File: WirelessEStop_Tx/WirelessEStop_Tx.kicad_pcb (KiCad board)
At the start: 2 copper layers, 99.1 x 99.1 mm, 0 parts

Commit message: Worked on Board Layout
Pretty much finished the board. Need the BOM and stuff yet.
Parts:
- added C1: 10u, Capacitor_SMD:C_0603_1608Metric_Pad1.05x0.95mm_HandSolder, F.Cu at (127.5, 97.0)
- added C2: 10u, Capacitor_SMD:C_0603_1608Metric_Pad1.05x0.95mm_HandSolder, F.Cu at (113.3, 95.5)
- added Conn1: 9V Batt, MRDT_Connectors:MOLEX_SL_02_Horizontal, B.Cu at (139.2, 78.1)
- added D0: 3.3V_Schottky, Diode_SMD:D_0603_1608Metric_Pad1.05x0.95mm_HandSolder, F.Cu at (119.8, 101.6)
- added D1: LED, LED_SMD:LED_0603_1608Metric_Pad1.05x0.95mm_HandSolder, F.Cu at (135.3, 112.0)
- added D2: LED, LED_SMD:LED_0603_1608Metric_Pad1.05x0.95mm_HandSolder, F.Cu at (142.5, 112.0)
- added D3: LED, LED_SMD:LED_0603_1608Metric_Pad1.05x0.95mm_HandSolder, F.Cu at (149.5, 112.0)
- added D4: LED, LED_SMD:LED_0603_1608Metric_Pad1.05x0.95mm_HandSolder, F.Cu at (156.8, 112.0)
- added D5: LED, LED_SMD:LED_0603_1608Metric_Pad1.05x0.95mm_HandSolder, F.Cu at (152.0, 89.7)
- added G***: LOGO, MRDT_Silkscreens:MRDT_Logo_20mm, F.Cu at (177.3, 87.6)
- added L1: 47uH Inductor, WirelessEStop:ETQ-P4M470YFN_Inductor, F.Cu at (127.4, 101.6)
- added R1: 10K, Resistor_SMD:R_0603_1608Metric_Pad1.05x0.95mm_HandSolder, F.Cu at (121.9, 112.7)
- added R2: 10K, Resistor_SMD:R_0603_1608Metric_Pad1.05x0.95mm_HandSolder, F.Cu at (121.9, 116.3)
- added R3: 500, Resistor_SMD:R_0603_1608Metric_Pad1.05x0.95mm_HandSolder, F.Cu at (142.5, 116.3)
- added R4: 500, Resistor_SMD:R_0603_1608Metric_Pad1.05x0.95mm_HandSolder, F.Cu at (149.6, 116.3)
- added R5: 500, Resistor_SMD:R_0603_1608Metric_Pad1.05x0.95mm_HandSolder, F.Cu at (156.7, 116.3)
- added R6: 500, Resistor_SMD:R_0603_1608Metric_Pad1.05x0.95mm_HandSolder, F.Cu at (152.1, 92.7)
- added R7: 500, Resistor_SMD:R_0603_1608Metric_Pad1.05x0.95mm_HandSolder, F.Cu at (135.4, 115.7)
- added SW1: MOM Switch, WirelessEStop:D6_SPST, F.Cu at (154.7, 73.3)
- added SW2: Maintain Switch, WirelessEStop:ToggleSwitch_SPDT, F.Cu at (172.6, 105.7)
- added SW3: Master Power, WirelessEStop:SlideSwitch_SPST, F.Cu at (98.3, 97.8)
- added U1: ESP_8266_01, WirelessEStop:ESP8266-01, F.Cu at (96.3, 117.9)
- added U2: AP1059, Package_SO:SOIC-8_3.9x4.9mm_P1.27mm, F.Cu at (113.3, 99.6)
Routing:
- net +3V3: track 0.00 -> 186.5 mm, vias 0 -> 6
- net Maintain_IN: track 0.00 -> 118.0 mm, vias 0 -> 2
- net MOM_IN: track 0.00 -> 100.8 mm, vias 0 -> 2
- net SW_EStop: track 0.00 -> 74.6 mm, vias 0 -> 4
- net /Vin: track 0.00 -> 53.5 mm
- net SW_Link_EN: track 0.00 -> 43.8 mm
- net Net-(D0-Pad1): track 0.00 -> 20.1 mm
- net Net-(C2-Pad2): track 0.00 -> 16.2 mm
- net Net-(D5-Pad1): track 0.00 -> 3.09 mm
- net Net-(D4-Pad1): track 0.00 -> 2.61 mm
- net Net-(D3-Pad1): track 0.00 -> 2.61 mm
- net Net-(D2-Pad1): track 0.00 -> 2.57 mm
- net Net-(D1-Pad1): track 0.00 -> 1.97 mm
- net GND: track 0.00 -> 0.41 mm, vias 0 -> 19
- added copper zone on B.Cu, net GND
- added copper zone on F.Cu, net GND
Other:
- board text added: "Dead Man's SW"
- board text added: "EStop"
- board text added: "Enable Estop"
- board text added: "Enable Estop SW"
- board text added: "Main Power"
- board text added: "Power"
- board text added: "Wifi Connection"

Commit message: Fixed Board
Changed AP1509 and fixed the ESP8266-01
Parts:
- removed D0: 3.3V_Schottky, Diode_SMD:D_0603_1608Metric_Pad1.05x0.95mm_HandSolder
- removed G***: LOGO, MRDT_Silkscreens:MRDT_Logo_20mm
- removed L1: 47uH Inductor, WirelessEStop:ETQ-P4M470YFN_Inductor
- U2: value AP1059 -> OKI; footprint Package_SO:SOIC-8_3.9x4.9mm_P1.27mm -> MRDT_Devices:OKI_Horizontal
- moved C1 9.98 mm to (120.5, 104.1)
- moved U2 9.16 mm to (121.9, 102.6), turned to 180 degrees
- moved C2 8.64 mm to (113.4, 104.1)
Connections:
- C1 pad 1: +3V3 -> GND
- C1 pad 2: GND -> Net-(C1-Pad2)
- C2 pad 2: Net-(C2-Pad2) -> +3V3
- SW3 pad 1: Net-(C2-Pad2) -> Net-(C1-Pad2)
- U2 pad 1: Net-(C2-Pad2) -> Net-(C1-Pad2)
- U2 pad 2: Net-(D0-Pad1) -> GND
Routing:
- net Net-(C1-Pad2): track 0.00 -> 27.4 mm
- net Maintain_IN: track 118.0 -> 97.5 mm
- net SW_EStop: track 74.6 -> 95.0 mm
- net Net-(D0-Pad1): track 20.1 -> 0.00 mm
- net Net-(C2-Pad2): track 16.2 -> 0.00 mm
- net +3V3: track 186.5 -> 191.1 mm, vias 6 -> 2
- net SW_Link_EN: track 43.8 -> 46.5 mm
- net MOM_IN: track 100.8 -> 99.5 mm
- net GND: track 0.41 -> 0.00 mm, vias 19 -> 14

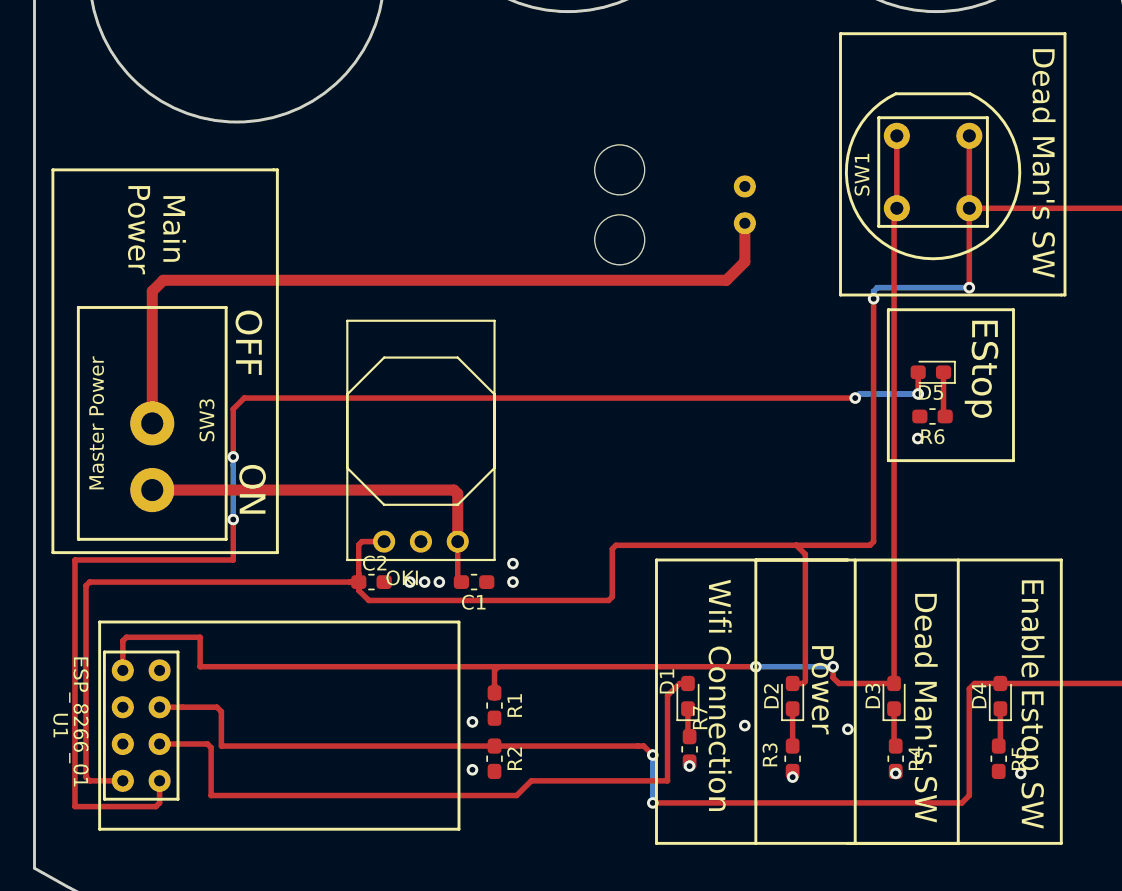
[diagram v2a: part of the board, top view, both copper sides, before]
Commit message: Updated BOM
Fixed the items on the BOM
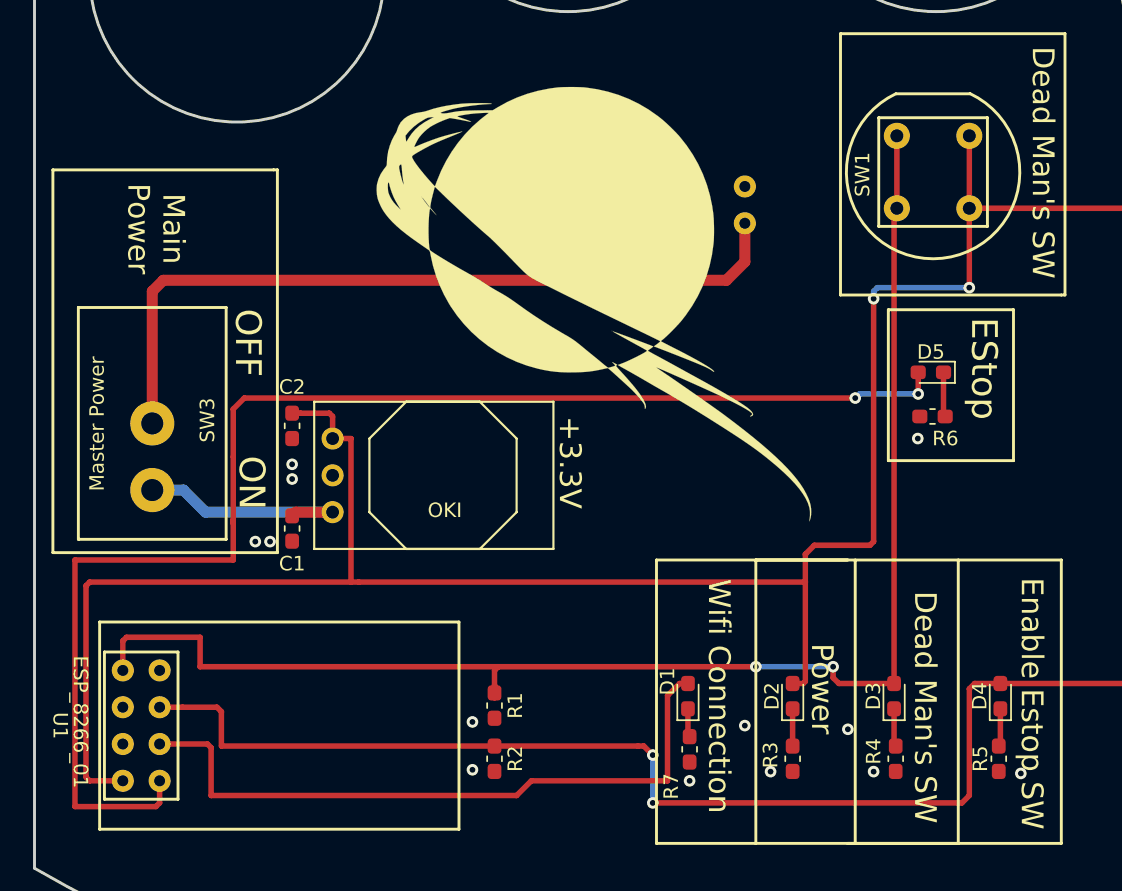
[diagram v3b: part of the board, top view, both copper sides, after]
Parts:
- added G***: LOGO, MRDT_Silkscreens:MRDT_Logo_30mm, F.Cu at (128.8, 85.0)
- Conn1: footprint MRDT_Connectors:MOLEX_SL_02_Horizontal -> WirelessEStop:MOLEX_SL_02_Horizontal_NoHole
- moved C1 13.1 mm to (108.0, 100.4), turned to 90 degrees
- moved U2 12.5 mm to (109.5, 101.9), turned to 90 degrees
- moved C2 12.1 mm to (108.0, 93.4), turned to 90 degrees
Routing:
- net Net-(C1-Pad2): track 27.4 -> 16.0 mm
- net +3V3: track 191.1 -> 196.6 mm
- net SW_EStop: track 95.0 -> 95.3 mm, vias 4 -> 2
- net GND: vias 14 -> 13
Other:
- board text added: "+3.3V"

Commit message: Fixed Gerbs?
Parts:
- added REF**: 0.8in_Diameter_Hole, MRDT_Drill_Holes:0.8in_Diameter_Hole, F.Cu at (104.1, 62.2)
- added REF**: 0.8in_Diameter_Hole, MRDT_Drill_Holes:0.8in_Diameter_Hole, F.Cu at (175.3, 62.2)
- added REF**: 0.8in_Diameter_Hole, MRDT_Drill_Holes:0.8in_Diameter_Hole, F.Cu at (127.0, 54.6)
- added REF**: 0.8in_Diameter_Hole, MRDT_Drill_Holes:0.8in_Diameter_Hole, F.Cu at (152.4, 54.6)
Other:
- outline, holes or cut-outs redrawn
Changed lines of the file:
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@@
   (general
     (thickness 1.6)
-    (drawings 59)
+    (drawings 55)
     (tracks 140)
     (zones 0)
-    (modules 21)
+    (modules 25)
     (nets 16)
   )
@@
   )
   (setup
-    (last_trace_width 0.381)
+    (last_trace_width 0.25)
     (user_trace_width 0.381)
     (user_trace_width 0.762)
@@
     (add_net SW_EStop)
     (add_net SW_Link_EN)
+  )
+  (module MRDT_Drill_Holes:0.8in_Diameter_Hole (layer F.Cu)
+    (at 104.14 62.23)
+    (fp_text reference REF** (at -0.00508 0.50508) (layer F.SilkS) hide
+      (effects (font (size 1 1) (thickness 0.15)))
+    )
+    (fp_text value 0.8in_Diameter_Hole (at 0.2 -11.1) (layer F.Fab) hide
+      (effects (font (size 1 1) (thickness 0.15)))
+    )
+    (pad "" np_thru_hole circle (at 0 0) (size 20.32 20.32) (drill 20.32) (layers *.Cu *.Mask))
+  )
+  (module MRDT_Drill_Holes:0.8in_Diameter_Hole (layer F.Cu)
+    (at 175.26 62.23)
+    (fp_text reference REF** (at -0.00508 0.50508) (layer F.SilkS) hide
+      (effects (font (size 1 1) (thickness 0.15)))
+    )
+    (fp_text value 0.8in_Diameter_Hole (at 0.2 -11.1) (layer F.Fab) hide
+      (effects (font (size 1 1) (thickness 0.15)))
+    )
+    (pad "" np_thru_hole circle (at 0 0) (size 20.32 20.32) (drill 20.32) (layers *.Cu *.Mask))
+  )
+  (module MRDT_Drill_Holes:0.8in_Diameter_Hole (layer F.Cu)
+    (at 127 54.61)
+    (fp_text reference REF** (at -0.00508 0.50508) (layer F.SilkS) hide
+      (effects (font (size 1 1) (thickness 0.15)))
+    )
+    (fp_text value 0.8in_Diameter_Hole (at 0.2 -11.1) (layer F.Fab) hide
+      (effects (font (size 1 1) (thickness 0.15)))
+    )
+    (pad "" np_thru_hole circle (at 0 0) (size 20.32 20.32) (drill 20.32) (layers *.Cu *.Mask))
   )
   (module WirelessEStop:MOLEX_SL_02_Horizontal_NoHole (layer B.Cu)
@@
       (xy 4.577283 -8.243201) (xy 4.607434 -8.26797) (xy 4.65957 -8.298902) (xy 4.678269 -8.298685)) (layer F.SilkS) (width 0.01))
   )
+  (module MRDT_Drill_Holes:0.8in_Diameter_Hole (layer F.Cu)
+    (at 152.4 54.61)
+    (fp_text reference REF** (at -0.00508 0.50508) (layer F.SilkS) hide
+      (effects (font (size 1 1) (thickness 0.15)))
+    )
+    (fp_text value 0.8in_Diameter_Hole (at 0.2 -11.1) (layer F.Fab) hide
+      (effects (font (size 1 1) (thickness 0.15)))
+    )
+    (pad "" np_thru_hole circle (at 0 0) (size 20.32 20.32) (drill 20.32) (layers *.Cu *.Mask))
+  )
   (gr_text +3.3V (at 127.127 95.885 270) (layer F.SilkS)
     (effects (font (size 1.5 1.5) (thickness 0.3)))
@@
   (gr_line (start 90.17 51.3715) (end 90.17 123.8885) (layer Edge.Cuts) (width 0.2))
   (gr_arc (start 139.7 137.16) (end 139.7 38.1) (angle -29.9999929) (layer Edge.Cuts) (width 0.2))
-  (gr_circle (center 127 54.61) (end 137.16 54.61) (layer Edge.Cuts) (width 0.2))
-  (gr_circle (center 152.4 54.61) (end 162.56 54.61) (layer Edge.Cuts) (width 0.2))
-  (gr_circle (center 175.26 62.23) (end 185.42 62.23) (layer Edge.Cuts) (width 0.2))
-  (gr_circle (center 104.14 62.23) (end 114.3 62.23) (layer Edge.Cuts) (width 0.2))
   (segment (start 154.686 73.3425) (end 154.686 78.3425) (width 0.381) (layer F.Cu) (net 1))
   (segment (start 147.828 101.6) (end 148.082 101.346) (width 0.381) (layer F.Cu) (net 1))

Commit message: Fixed Errors and made neater
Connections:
- SW2 pad 1: +3V3 -> GND
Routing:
- net +3V3: track 196.6 -> 184.8 mm
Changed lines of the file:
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@@
     (thickness 1.6)
     (drawings 55)
-    (tracks 140)
+    (tracks 137)
     (zones 0)
     (modules 25)
@@
     (mod_text_size 1 1)
     (mod_text_width 0.15)
-    (pad_size 1.524 1.524)
-    (pad_drill 0.762)
+    (pad_size 3.81 3.81)
+    (pad_drill 2.08)
     (pad_to_mask_clearance 0.2)
     (aux_axis_origin 0 0)
@@
       (net 2 Maintain_IN))
     (pad 1 thru_hole circle (at 0 0) (size 3.81 3.81) (drill 2.08) (layers *.Cu *.Mask)
-      (net 1 +3V3))
+      (net 6 GND))
   )
   (module WirelessEStop:D6_SPST (layer F.Cu)
@@
   (segment (start 181.992 102.969924) (end 181.864 102.841924) (width 0.381) (layer F.Cu) (net 1))
   (segment (start 181.992 105.664) (end 181.992 102.969924) (width 0.381) (layer F.Cu) (net 1))
-  (segment (start 172.592 105.664) (end 172.592 103.25) (width 0.381) (layer F.Cu) (net 1))
-  (segment (start 173.000076 102.841924) (end 181.864 102.841924) (width 0.381) (layer F.Cu) (net 1))
-  (segment (start 172.592 103.25) (end 173.000076 102.841924) (width 0.381) (layer F.Cu) (net 1))
   (segment (start 108.525 92.484) (end 107.95 92.484) (width 0.381) (layer F.Cu) (net 1))
   (segment (start 110.518 92.484) (end 108.525 92.484) (width 0.381) (layer F.Cu) (net 1))

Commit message: Tiny update
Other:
- board text added: "Wireless E-Stop Transmitter Mars Rover, Valkyrie Missouri S&T Andrew Simily"
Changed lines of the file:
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@@
   (general
     (thickness 1.6)
-    (drawings 55)
+    (drawings 56)
     (tracks 137)
     (zones 0)
@@
     (pad "" np_thru_hole circle (at 0 0) (size 20.32 20.32) (drill 20.32) (layers *.Cu *.Mask))
   )
+  (gr_text "Wireless E-Stop Transmitter\nMars Rover, Valkyrie\nMissouri S&T\nAndrew Simily" (at 146.685 128.651) (layer F.SilkS)
+    (effects (font (size 1.5 1.5) (thickness 0.3)))
+  )
   (gr_text +3.3V (at 127.127 95.885 270) (layer F.SilkS)
